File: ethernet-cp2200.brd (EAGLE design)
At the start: 55.5 x 39.4 mm, 21 parts, among them IC1 CP2200-GQ, Q1 20MHz

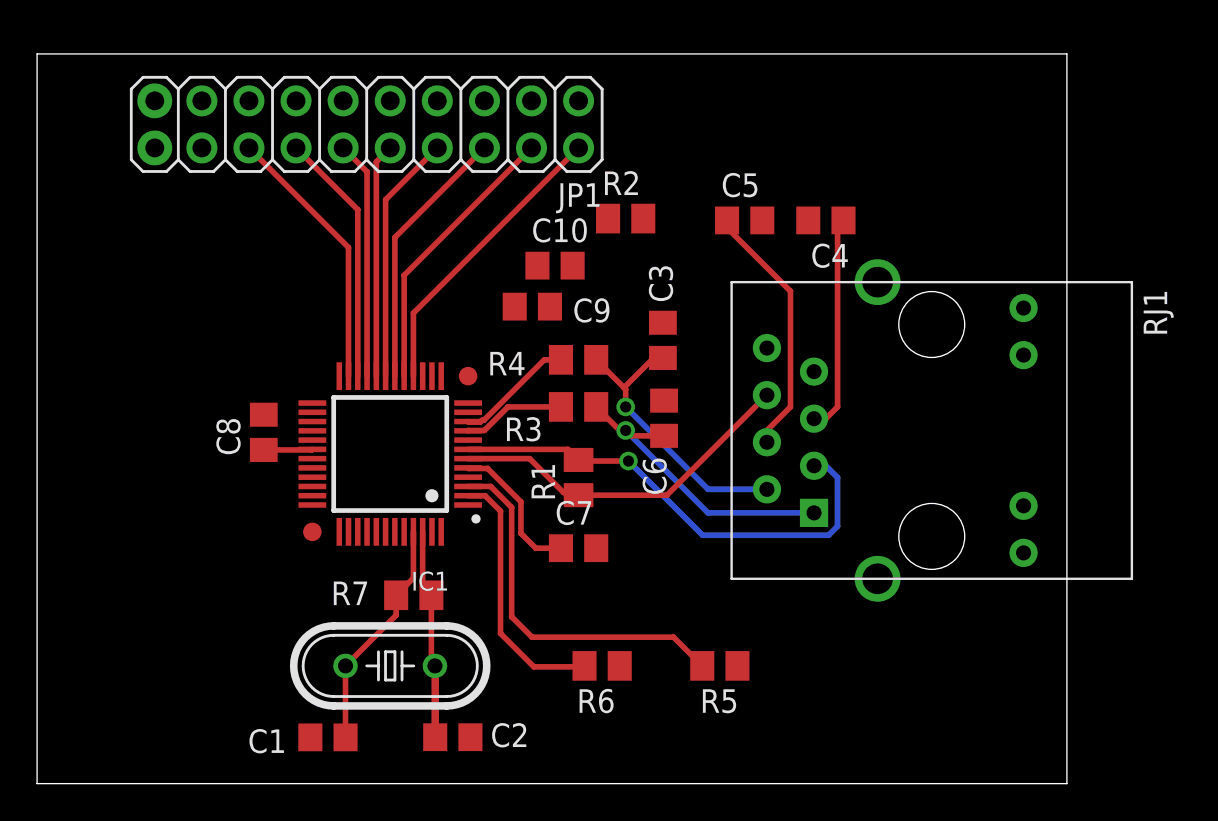
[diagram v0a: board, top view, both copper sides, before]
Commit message: Connected the cp2200 board
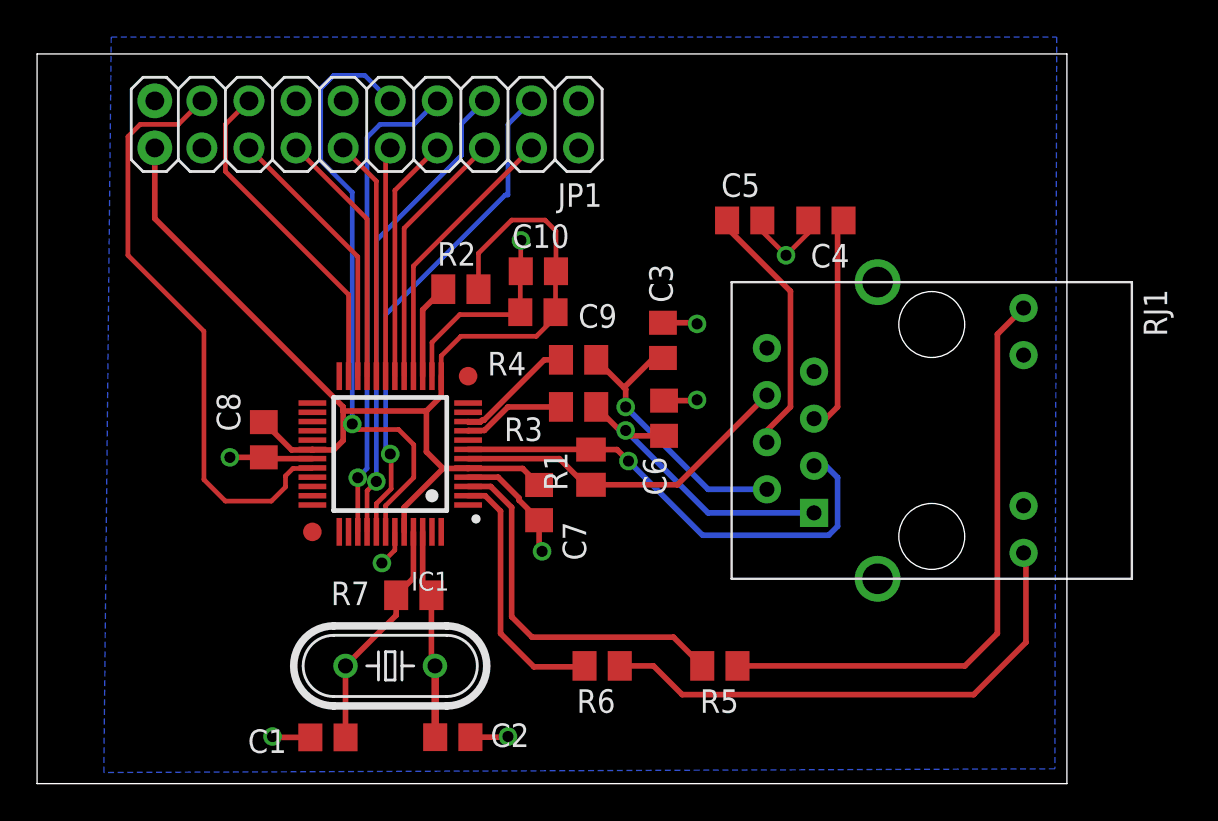
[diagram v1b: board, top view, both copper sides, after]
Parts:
- moved R2 9.67 mm to (22.9, 26.7)
- moved C7 3.25 mm to (27.1, 15.2), turned to 270 degrees
- moved C10 0.95 mm to (27.0, 27.6), turned to 180 degrees
- moved R1 0.87 mm to (29.9, 17.1)
- moved C9 0.42 mm to (27.0, 25.4)
- moved C8 0.40 mm to (12.2, 18.6), turned to 270 degrees
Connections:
- removed net N$17: IC1.14, IC1.31, IC1.4
- removed net N$24: IC1.23, JP1.16
- new net N$11: IC1.32, JP1.17
- new net N$13: IC1.16, JP1.4
- net GND: now also IC1.14, IC1.31, IC1.4
- net N$16: now also IC1.17, JP1.6; no longer IC1.16, JP1.2
- net N$18: now also IC1.18, JP1.8; no longer IC1.17, JP1.4
- net N$19: now also IC1.19, JP1.10; no longer IC1.18, JP1.6
- net N$20: now also IC1.20, JP1.12; no longer IC1.19, JP1.8
- net N$21: now also IC1.21, JP1.14; no longer IC1.20, JP1.10
- net N$22: now also IC1.22, JP1.16; no longer IC1.21, JP1.12
- net N$23: now also IC1.23, JP1.15; no longer IC1.22, JP1.14
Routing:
- net +3V3: track 10.4 -> 65.0 mm
- net GND: track 0.00 -> 36.7 mm, vias 0 -> 9
- net N$9: track 0.00 -> 32.9 mm
- net N$28: track 0.00 -> 32.5 mm, vias 0 -> 1
- net N$11: track 0.00 -> 32.4 mm
- net N$10: track 0.00 -> 28.6 mm
- net N$25: track 0.00 -> 27.1 mm, vias 0 -> 1
- net N$27: track 0.00 -> 26.1 mm, vias 0 -> 1
- net N$26: track 0.00 -> 25.9 mm, vias 0 -> 1
- net N$13: track 0.00 -> 14.9 mm
- net N$24: track 14.5 -> 0.00 mm
- net N$29: track 0.00 -> 5.15 mm
- net N$23: track 13.7 -> 18.1 mm
- net N$22: track 12.8 -> 14.7 mm
- net N$18: track 15.2 -> 13.3 mm
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- added copper zone on layer 16, net GND

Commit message: Updated board after drc
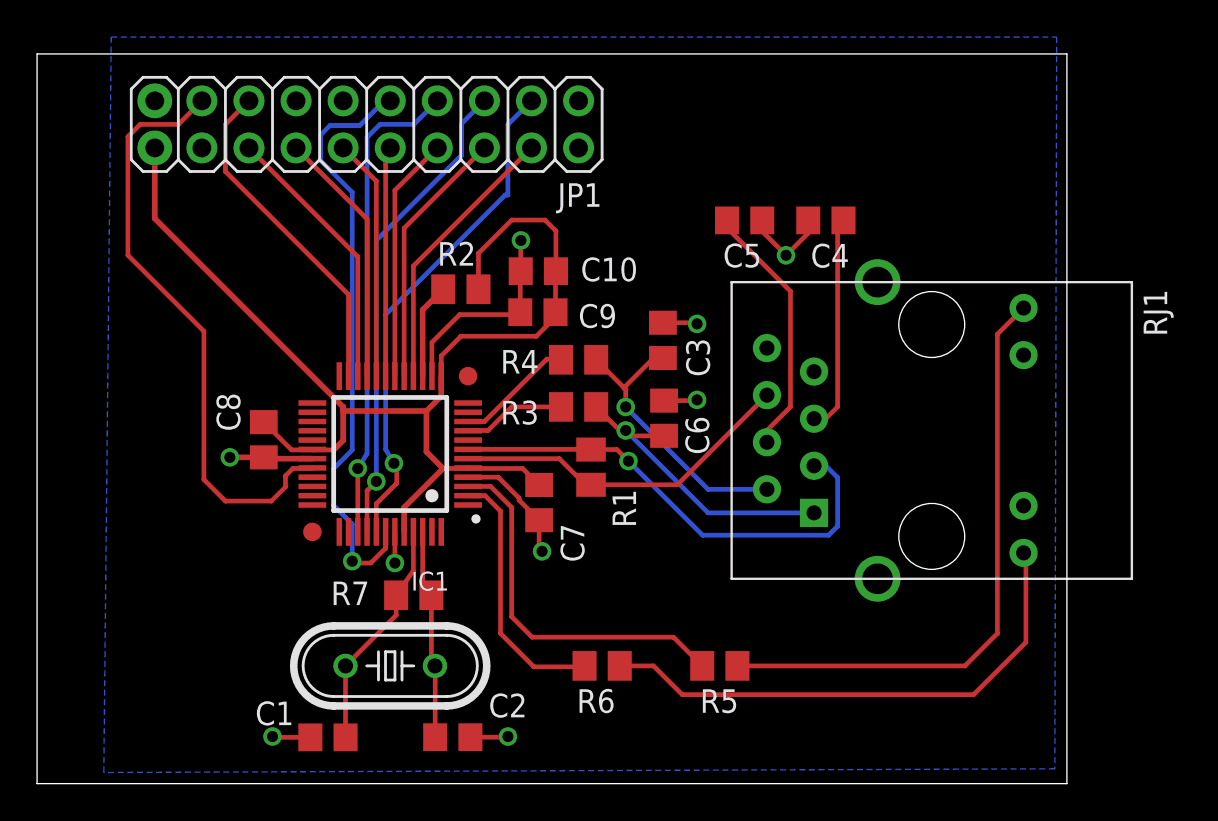
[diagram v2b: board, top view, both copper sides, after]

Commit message: Fixing smd pad width and some wire traces and adding text
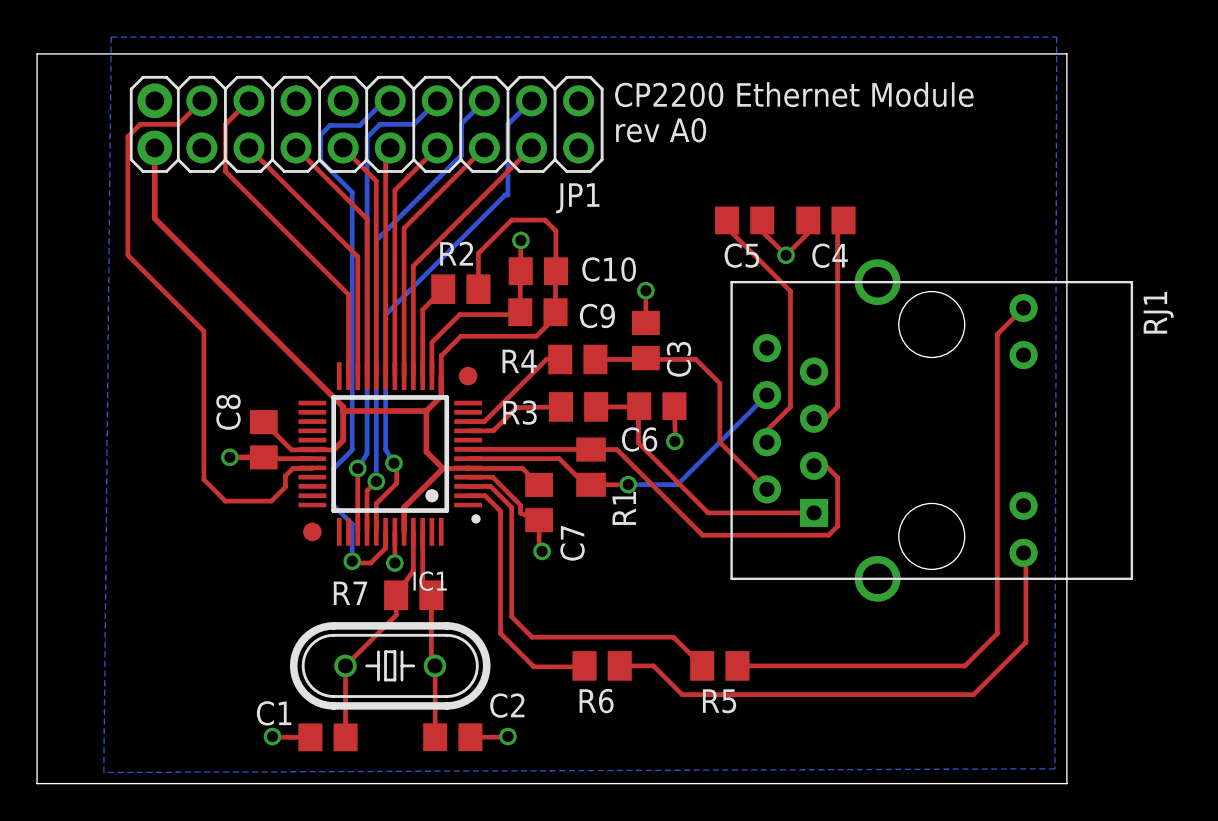
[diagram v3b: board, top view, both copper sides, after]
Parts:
- moved C3 0.92 mm to (32.8, 23.9)
- moved C6 0.76 mm to (33.4, 20.4), turned to 0 degrees
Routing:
- net N$12: track 15.4 -> 14.1 mm, vias 1 -> 0
- net N$7: track 16.3 -> 15.3 mm, vias 1 -> 0
- net N$4: vias 0 -> 1
- net N$5: vias 1 -> 0
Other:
- board text added: "CP2200 Ethernet Module rev A0"
